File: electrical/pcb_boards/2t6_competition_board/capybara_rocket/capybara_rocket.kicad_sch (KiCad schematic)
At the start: 28 parts, among them J1 Conn_01x08_Pin, J10 Wurth_M4_62000411622, J11 Wurth_M4_62000411622, J12 Wurth_M3_62000311622, J13 Wurth_M3_62000311622, J14 Wurth_M3_62000311622, J15 Wurth_M3_62000311622, J16 Wurth_M3_62000311622, J17 Wurth_M3_62000311622, J2 Conn_01x06_Pin, J3 Wurth_M2_62000211622, J4 Wurth_M2_62000211622, J5 Wurth_M2_62000211622, J6 Wurth_M2_62000211622, J7 Wurth_M2_62000211622, J9 Wurth_M4_62000411622, U1 WRL-11812, U2 4754, U3 VL53L1-SATEL, U4 NUCLEO-G431KB, U5 DS1307+, U6 NE555P, U7 25LC1024-E/P, U8 DRV8212DRLR, U9 SN74LVC1G04DBVR, Y1 AB38T-32.768KHZ

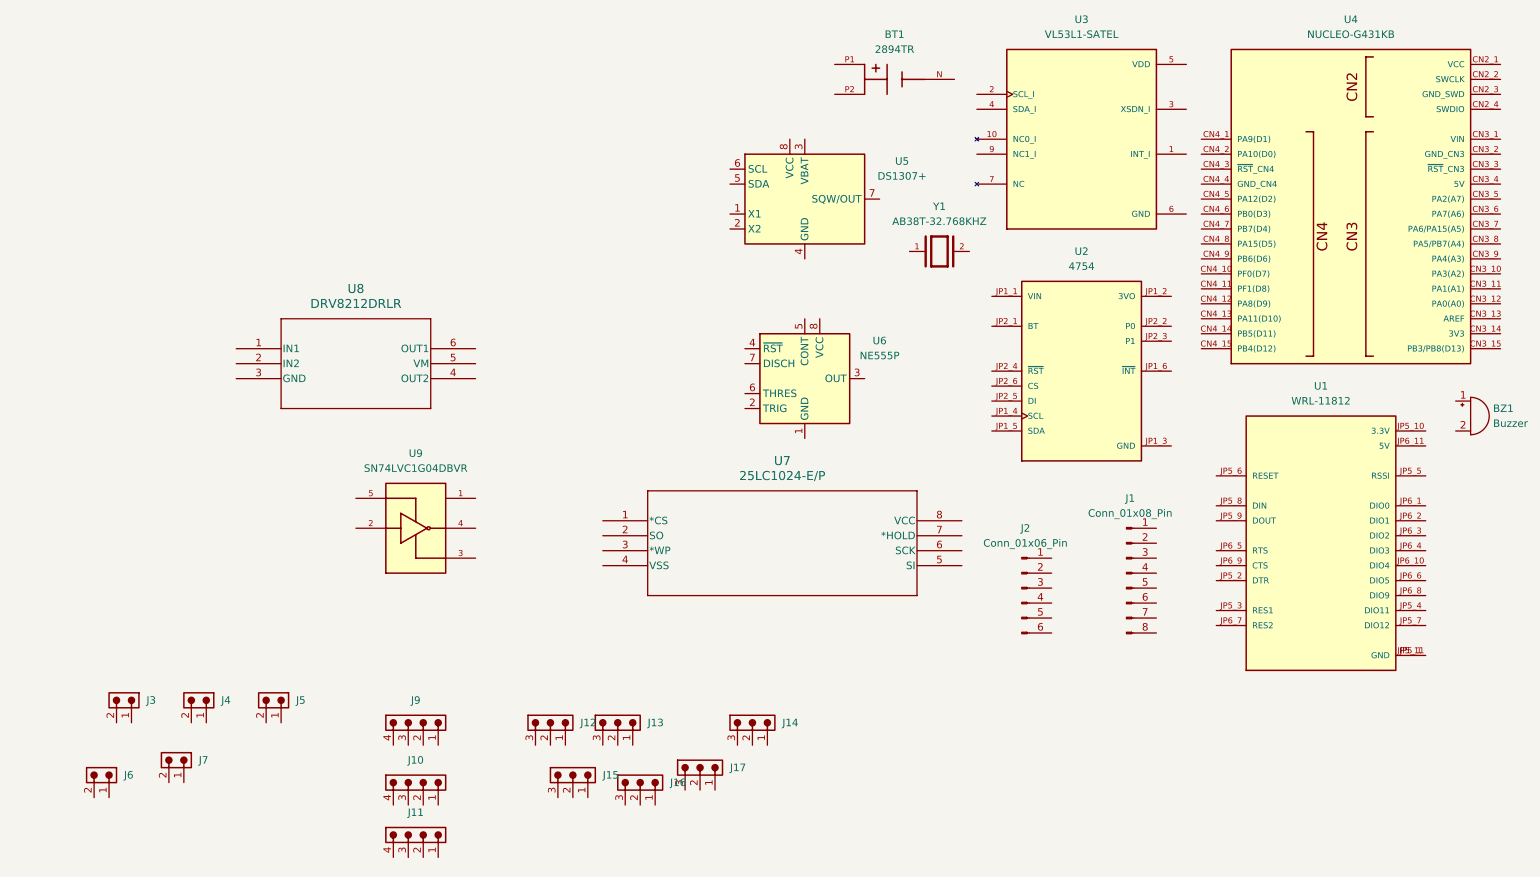
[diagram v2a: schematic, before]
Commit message: Adding buck boost components
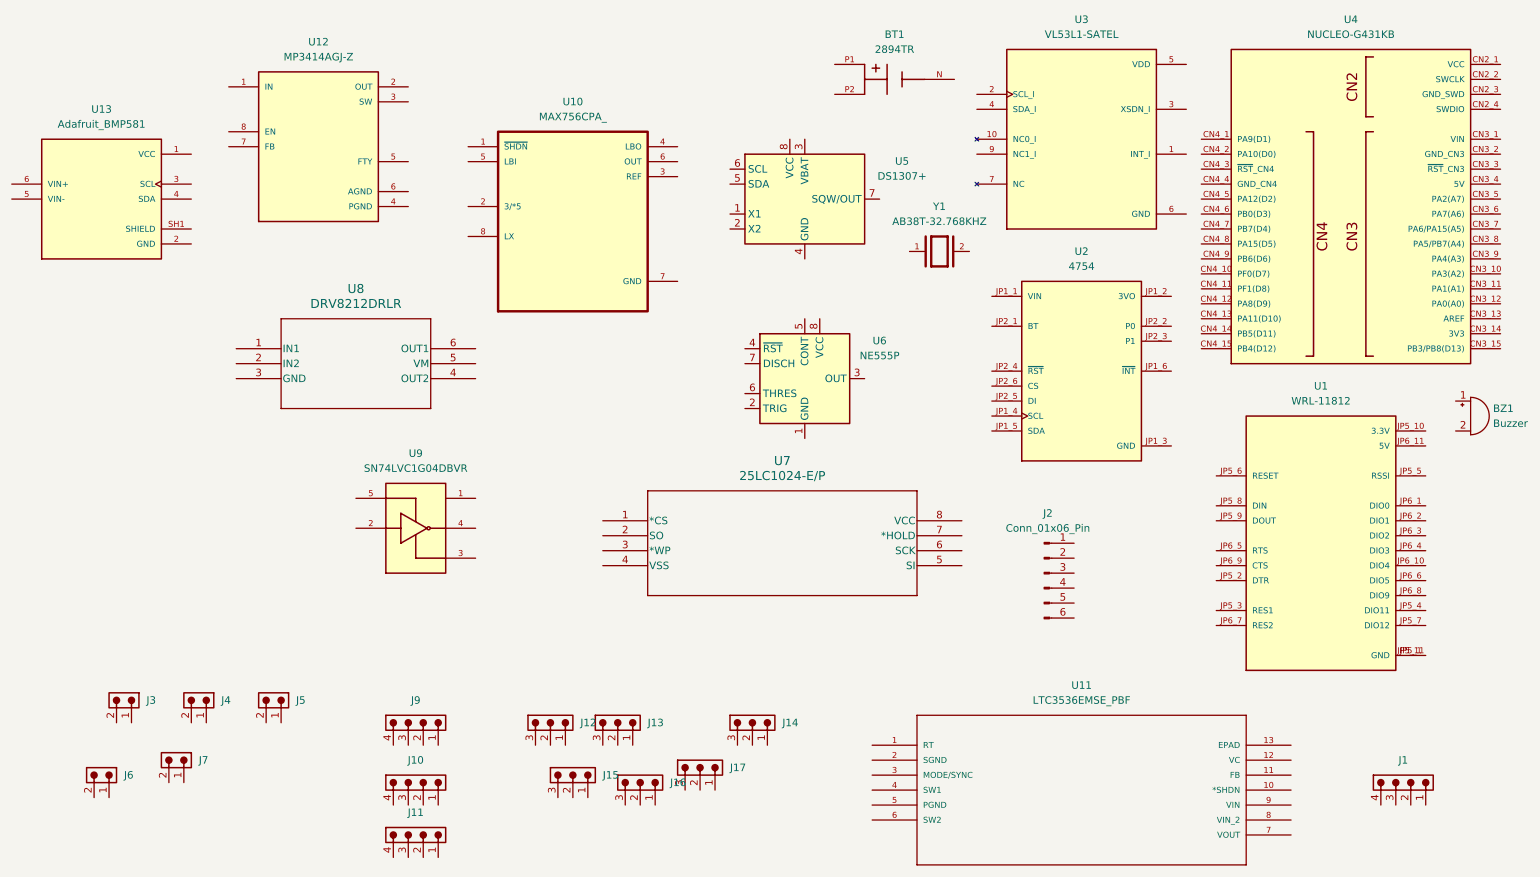
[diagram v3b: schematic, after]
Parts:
- removed J1: Conn_01x08_Pin, RSX_CanSat_Custom_KiCad_Footprints:Adafruit_BMP581, symbol Connector:Conn_01x08_Pin
- added J1: Wurth_M4_62000411622, RSX_CanSat_Custom_KiCad_Footprints:SparkFun_GNSS_MAX_M10S, symbol RSX_CanSat_Custom_KiCad_Symbols:Wurth_M4_62000411622
- added U10: MAX756CPA_, RSX_CanSat_Custom_KiCad_Footprints:DIP794W47P254L991H457Q8, symbol RSX_CanSat_Custom_KiCad_Symbols:MAX756CPA_
- added U11: LTC3536EMSE_PBF, RSX_CanSat_Custom_KiCad_Footprints:MSOP-12_MSE, symbol RSX_CanSat_Custom_KiCad_Symbols:LTC3536EMSE_PBF
- added U12: MP3414AGJ-Z, RSX_CanSat_Custom_KiCad_Footprints:TSOT23-8_MP3414A, symbol RSX_CanSat_Custom_KiCad_Symbols:MP3414AGJ-Z
- added U13: Adafruit_BMP581, RSX_CanSat_Custom_KiCad_Footprints:Adafruit_BMP581, symbol RSX_CanSat_Custom_KiCad_Symbols:Adafruit_BMP581
- J2: footprint RSX_CanSat_Custom_KiCad_Footprints:MODULE_904 -> RSX_CanSat_Custom_KiCad_Footprints:Adafruit_INA219
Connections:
- new net: U13.5 (VIN-), U13.VIN-
- new net: U13.6 (VIN+), U13.VIN+
- new net: U13.SH1 (SHIELD), U13.SH2 (SHIELD), U13.SH3 (SHIELD), U13.SH4 (SHIELD)
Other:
- moved on the sheet: J2

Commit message: Major CPL PCB work update
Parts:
- added C1, C2: 10μF, Capacitor_SMD:C_0805_2012Metric_Pad1.18x1.45mm_HandSolder, symbol Device:C
- added C3, C4, C5, C6, C7, C8: 0.1μF, Capacitor_SMD:C_0805_2012Metric_Pad1.18x1.45mm_HandSolder, symbol Device:C
- added R1, R4: 10Ω, Resistor_SMD:R_0603_1608Metric_Pad0.98x0.95mm_HandSolder, symbol Device:R
- added R2: 220Ω, Resistor_SMD:R_0603_1608Metric_Pad0.98x0.95mm_HandSolder, symbol Device:R
- added R3: 1kΩ, Resistor_SMD:R_0603_1608Metric_Pad0.98x0.95mm_HandSolder, symbol Device:R
- added TP1: TestPoint, symbol Connector:TestPoint
- J1: value Wurth_M4_62000411622 -> SparkFun MAX-M10S
- J2: value Conn_01x06_Pin -> Adafruit INA219
- U13: value Adafruit_BMP581 -> Adafruit BMP581
- U2: value 4754 -> Adafruit BNO085
- U4: value NUCLEO-G431KB -> STM32 NUCLEO-G431KB
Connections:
- net GND: now reaches BT1.N
- net GND: now also BZ1.2 (-), J1.1, J2.2 (Pin_2), J3.2, J4.2, J5.2, U1.JP5_1 (GND), U1.JP5_11 (GND), U13.2 (GND), U2.JP1_3 (GND), U3.6 (GND), U4.CN3_2 (GND_CN3), U5.4 (GND), U6.1 (GND), C1.2, C2.2, C3.2, C4.1, C5.1, C6.1, C7.2, C8.2
- net at BT1.P1: now also BT1.P2, U5.3 (VBAT)
- net 3.3V: now reaches U1.JP5_10 (3.3V)
- net 3.3V: now also J1.2, J2.1 (Pin_1), U13.1 (VCC), U2.JP1_1 (VIN), U3.5 (VDD), C4.2, C5.2, C6.2, C7.1, C8.1
- net XBEE_TX: now reaches U1.JP5_8 (DIN)
- net XBEE_TX: now also U4.CN4_1 (XBEE_TX(PA9(D1)))
- net XBEE_RX: now reaches U1.JP5_9 (DOUT)
- net XBEE_RX: now also U4.CN4_2 (XBEE_RX(PA10(D0)))
- net SDA: now reaches J1.3
- net SDA: now also J2.4 (Pin_4), U13.4 (SDA), U3.4 (SDA_I), U4.CN4_7 (I2C_SDA(PB7(D4))), U5.5 (SDA)
- net SCL: now reaches J1.4
- net SCL: now also J2.3 (Pin_3), U13.3 (SCL), U3.2 (SCL_I), U4.CN4_8 (I2C_SCL(PA15(D5))), U5.6 (SCL)
- net SCLK: now reaches U2.JP1_4 (SCL)
- net SCLK: now also U4.CN3_8 (SPI_SCK(PA5/PB7(A4)))
- net MISO: now reaches U2.JP1_5 (SDA)
- net MISO: now also U4.CN3_7 (SPI_MISO(PA6/PA15(A5)))
- net MOSI: now reaches U2.JP2_5 (DI)
- net MOSI: now also U4.CN3_6 (SPI_MOSI(PA7(A6)))
- net CS: now reaches U2.JP2_6 (CS)
- net CS: now also U4.CN3_9 (SPI_CS(PA4(A3)))
- net 5V: now reaches J5.1
- net 5V: now also J4.1, U5.8 (VCC), U6.4 (~{RST}), U6.8 (VCC), C3.1, R2.2
- net at U6.2 (TRIG): now also U6.6 (THRES), C1.1, R3.2
- net at U6.3 (OUT): now also R1.1
- net at U6.5 (CONT): now also C2.1
- net at U6.7 (DISCH): now also R2.1, R3.1
- net X1: now reaches Y1.1
- net X1: now also U5.1 (X1)
- net X2: now reaches Y1.2
- net X2: now also U5.2 (X2)
- net at BZ1.1 (+): now also R1.2
- net at J3.1: now also R4.1
- no-connect marks 0 -> 11
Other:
- note added: "Accelerometer Sensor Circuit"
- note added: "Barometer Sensor Circuit"
- note added: "Buzzer Circuit"
- note added: "GNSS Sensor Circuit"
- note added: "Ground Distance Sensor Circuit"
- note added: "Power Management"
- note added: "Time Chip Circuit"
- note added: "Voltage/Current Sensor Circuit"
- company: (none) -> Robotics of Space Exploration (RSX), University of Toronto
- title: (none) -> RSX Aerial CanSat 2T6 Payload PCB Design
- moved on the sheet: BT1, BZ1, J1, J10, J11, J12, J13, J14, J15, J16, J17, J2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

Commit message: March 8th updates
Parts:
- removed J2: Adafruit INA219, RSX_CanSat_Custom_KiCad_Footprints:Adafruit_INA219, symbol Connector:Conn_01x06_Pin
- removed U3: VL53L1-SATEL, RSX_CanSat_Custom_KiCad_Footprints:J_Wurth_WR-WTB_62000411622, symbol RSX_CanSat_Custom_KiCad_Symbols:VL53L1-SATEL
- added D1, D2, D3, D4, D5: LED, DigiKey:WL-SMCW_0603, symbol Device:LED
- added J2: VL53L1-SATEL, RSX_CanSat_Custom_KiCad_Footprints:J_Wurth_WR-WTB_62000411622, symbol RSX_CanSat_Custom_KiCad_Symbols:Wurth_M4_62000411622
- added R5, R6: 2.2kΩ, Resistor_SMD:R_0603_1608Metric_Pad0.98x0.95mm_HandSolder, symbol Device:R
- added R7: PT2512FK-070R1L, RSX_CanSat_Custom_KiCad_Footprints:RESC6331X65N, symbol RSX_CanSat_Custom_KiCad_Symbols:PT2512FK-070R1L
- added U14: INA219BIDR, RSX_CanSat_Custom_KiCad_Footprints:SOIC127P599X175-8N, symbol RSX_CanSat_Custom_KiCad_Symbols:INA219BIDR
- BZ1: footprint Buzzer_Beeper:Buzzer_12x9.5RM7.6 -> RSX_CanSat_Custom_KiCad_Footprints:Buzzer_12x9.5RM7.6
- U10: footprint RSX_CanSat_Custom_KiCad_Footprints:DIP794W47P254L991H457Q8 -> Package_DIP:DIP-8_W7.62mm
- U7: footprint RSX_CanSat_Custom_KiCad_Footprints:PDIP8_300MC_MCH -> Package_DIP:DIP-8_W7.62mm
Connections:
- net 3.3V: now also C5.1, C8.2, U4.CN3_1 (VIN), J2.2, R5.1, R6.2, U14.5 (VS); no longer C5.2, C8.1
- net GND: now also C5.2, C8.1, U4.CN4_4 (GND_CN4), J2.1, U14.6 (GND); no longer C5.1, C8.2
- net SCL: now also J2.4, R6.1, U14.4 (SCL)
- net SDA: now also J2.3, R5.2, U14.3 (SDA)
- net WING_PWM: now reaches U4.CN3_11 (WING_PWM(PA1(A1)))
- net WING_DIR: now reaches U4.CN3_12 (WING_DIR(PA0(A0)))
- net G_CAM_OUT: now reaches U4.CN4_10 (G_CAM_OUT(PF0(D7)))
- net PG_CAM_OUT: now reaches U4.CN4_11 (PG_CAM_OUT(PF1(D8)))
- net PG_CAM_IN: now reaches U4.CN4_12 (PG_CAM_IN(PA8(D9)))
- net CC_REL: now reaches U4.CN4_13 (CC_REL(PA11(D10)))
- net AILERON: now reaches U4.CN4_14 (AILERON(PB5(D11)))
- net ELEVATOR: now reaches U4.CN4_15 (ELEVATOR(PB4(D12)))
- net NC_REL: now reaches U4.CN4_5 (NC_REL(PA12(D2)))
- net EGG_REL: now reaches U4.CN4_6 (EGG_REL(PB0(D3)))
- net G_CAM_IN: now reaches U4.CN4_9 (G_CAM_IN(PB6(D6)))
- new net: R7.1, U14.7 (VIN-)
- new net 3.6V: R7.2, U14.8 (VIN+)
- no-connect marks 11 -> 33
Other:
- note added: "I2C Pull-Up Circuit"
- note added: "Microcontroller Circuit"
- note added: "XBee Circuit"
- moved on the sheet: C5, C6, C7, C8, U1, U13, U4
